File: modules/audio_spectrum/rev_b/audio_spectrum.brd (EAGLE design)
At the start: 68.1 x 66 mm, 86 parts, among them J1 MODULE_GENERIC, J2 AUDIO-JACK-VERTICAL, J7 TC2030-JLINK-L, P1 4k-200k, P2 4k-200k, Q1 NX3008PBK, Q2 NX3008PBK, U1 SAM4LC8AA, U2 MSGEQ7, U3 MSGEQ7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

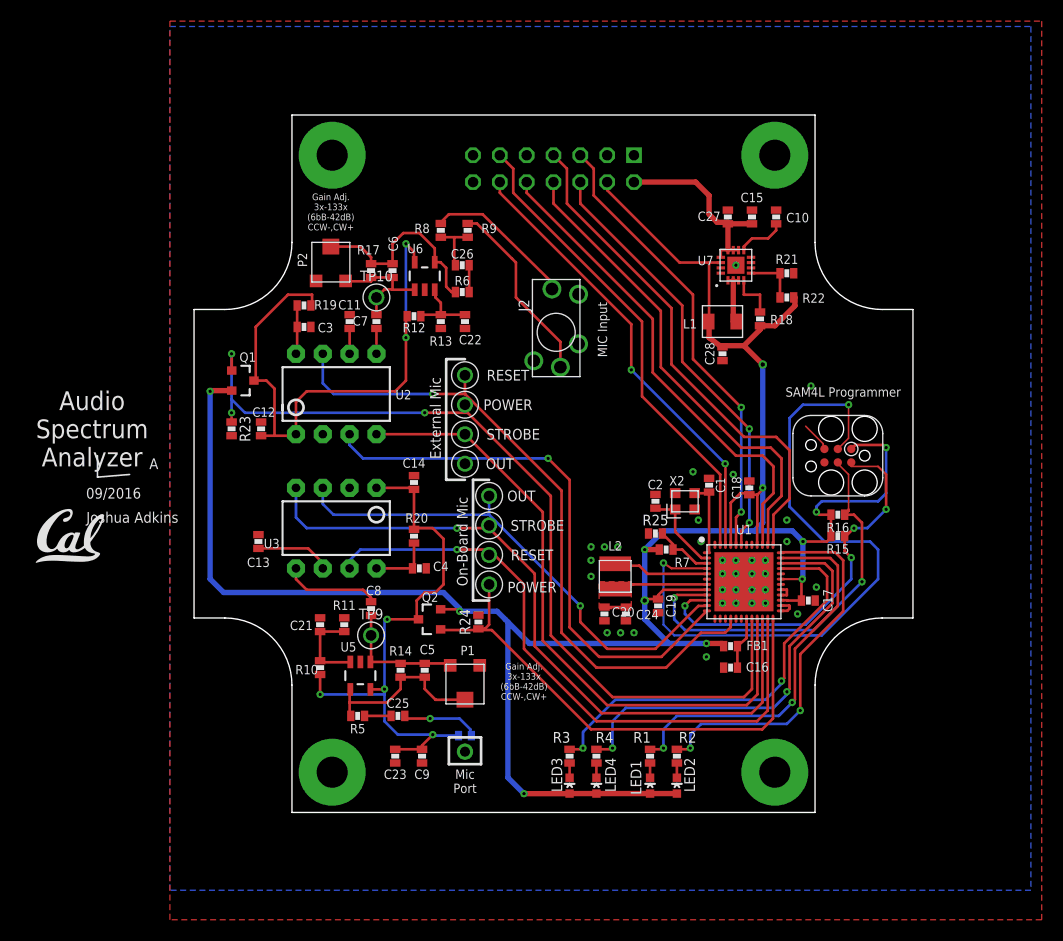
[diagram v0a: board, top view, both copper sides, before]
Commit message: updated audio spectrum board
-fixed the msgeq7 schematic bug
-tried to change layout of the switching stuff
-added some more dnp/populate messages
-added testpoints
-generally rerouted some traces
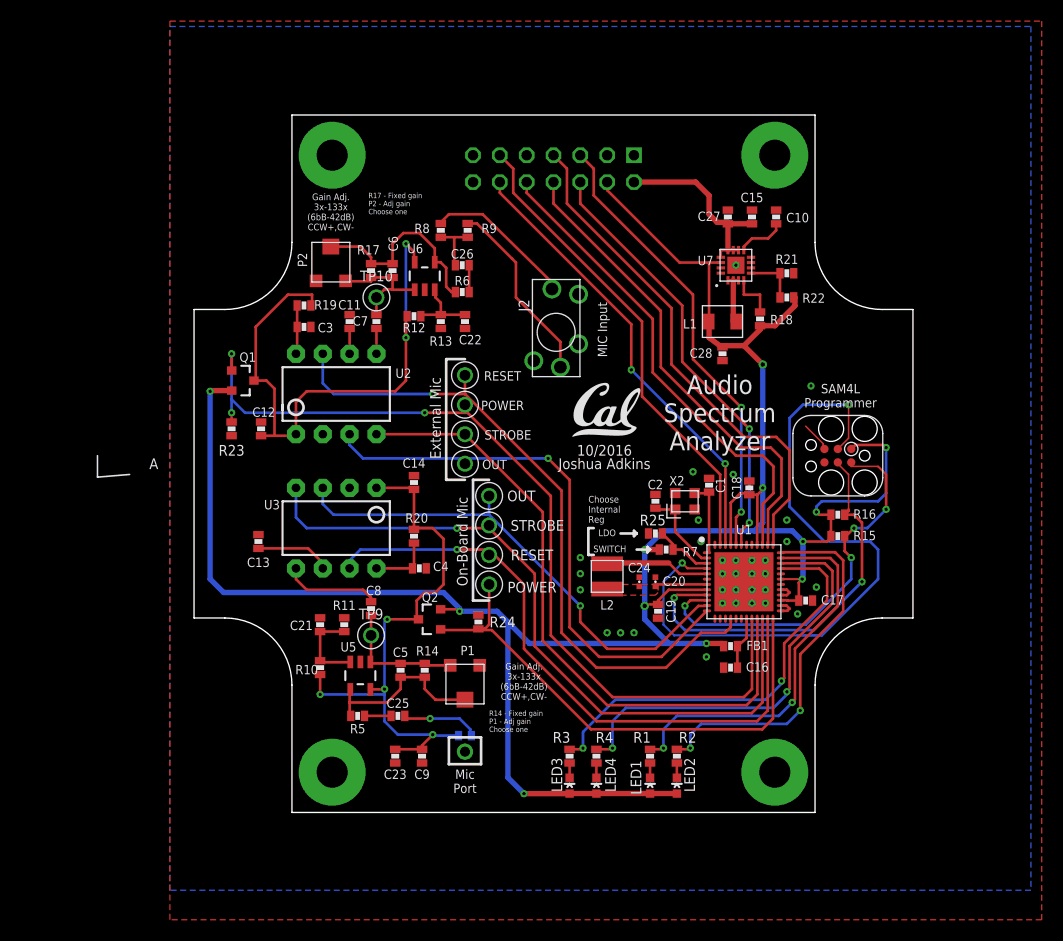
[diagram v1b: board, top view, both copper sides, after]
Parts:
- C20, C24: device passives:0603_CAP -> passives:0402_CAP
- moved U$2 52.2 mm to (38.4, 38.1)
- moved C20 5.71 mm to (46.2, 24.4), turned to 90 degrees
- moved C24 3.30 mm to (44.7, 24.4), turned to 90 degrees
- moved C5 2.29 mm to (22.1, 16.0)
- moved R14 2.29 mm to (24.4, 16.0)
- moved L2 0.76 mm to (41.7, 24.9)
- moved C19 0.51 mm to (46.5, 21.6)
- moved C17 0.25 mm to (60.5, 22.6)
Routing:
- net N$44: track 10.8 -> 4.95 mm
- net !CONTROLLER_RESET: track 65.1 -> 64.1 mm
- net N$52: track 9.09 -> 10.0 mm
- net GND: vias 39 -> 37
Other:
- board text added: "10/2016"
- board text added: "Choose Internal Reg"
- board text added: "Gain Adj. 3x-133x (6bB-42dB) CCW+,CW-"
- board text added: "LDO"
- board text added: "R14 - Fixed gain P1 - Adj gain Choose one"
- board text added: "R17 - Fixed gain P2 - Adj gain Choose one"
- board text added: "SWITCH"
- board text removed: "09/2016"
- board text removed: "Gain Adj. 3x-133x (6bB-42dB) CCW-,CW+"

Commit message: updated audio board layout
-added reset button
-more testpoints
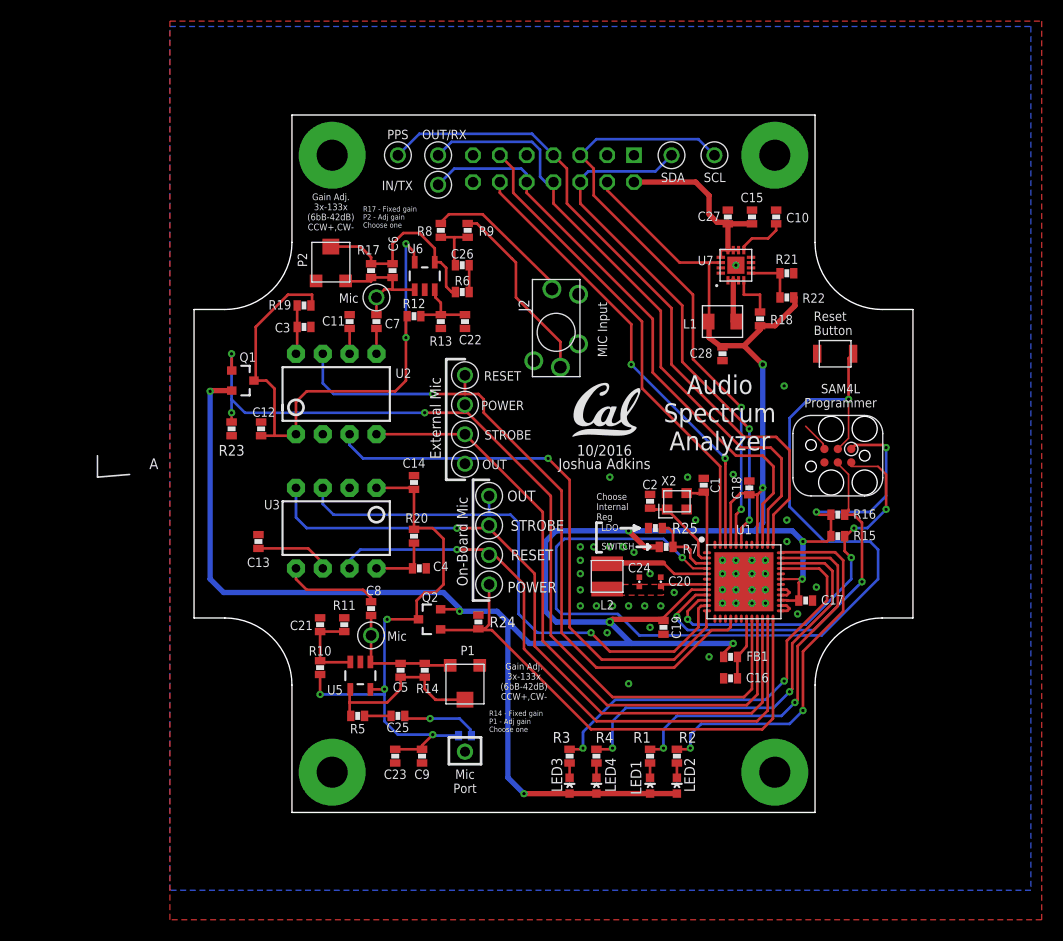
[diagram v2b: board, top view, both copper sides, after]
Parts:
- added S1: B3U-1000P, switches:B3U-1000P
- added TP12, TP13, TP14, TP15, TP16: TEST_POINT_0.040IN, headers:TESTPOINT_0.040IN
- moved C19 1.61 mm to (47.0, 20.1)
- moved FB1 1.02 mm to (53.3, 17.3)
- moved C16 1.02 mm to (53.3, 15.2)
- moved X2 0.76 mm to (48.3, 32.0)
- moved C1 0.51 mm to (50.8, 33.5)
- moved C2 0.51 mm to (45.7, 32.0)
- moved R25 0.51 mm to (46.2, 29.5)
- moved C20 0.51 mm to (46.7, 24.4)
- moved R7 0.25 mm to (47.2, 27.7)
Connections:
- net !CONTROLLER_RESET: now also S1.2
- net GND: now also S1.1
- net MOD_IN: now also TP14.TESTPOINT
- net MOD_OUT: now also TP15.TESTPOINT
- net PPS: now also TP16.TESTPOINT
- net SCL: now also TP12.TESTPOINT
- net SDA: now also TP13.TESTPOINT
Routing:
- net !CONTROLLER_RESET: track 64.1 -> 92.5 mm
- net 3V3: track 235.3 -> 258.9 mm
- net PPS: track 48.6 -> 65.0 mm
- net MOD_OUT: track 45.5 -> 60.0 mm
- net SCL: track 43.4 -> 57.4 mm
- net MOD_IN: track 46.0 -> 55.9 mm
- net SDA: track 41.3 -> 51.1 mm
- net SPEC_OUT: track 48.0 -> 53.4 mm
- net CONTROLLER_SWDCLK: track 38.4 -> 37.0 mm
- net CONTROLLER_BUCK/LDO_N: track 5.70 -> 6.87 mm
- net SPEC2_OUT: track 53.7 -> 54.8 mm
- net N$32: track 5.03 -> 5.97 mm
- net SPEC2_RESET: track 64.6 -> 65.4 mm
- net CONTROLLER_SWDIO: track 37.6 -> 37.1 mm
- net N$44: track 4.95 -> 4.45 mm
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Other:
- board text added: "IN/TX"
- board text added: "Mic"
- board text added: "OUT/RX"
- board text added: "PPS"
- board text added: "Reset Button"
- board text added: "SCL"
- board text added: "SDA"

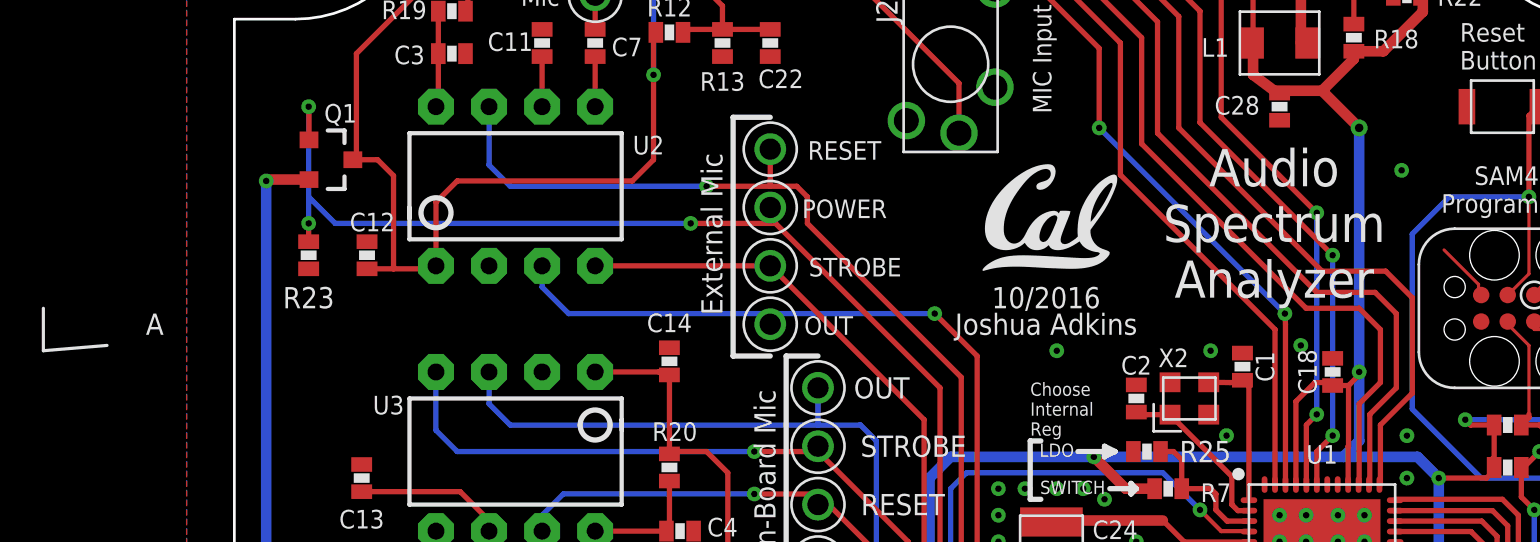
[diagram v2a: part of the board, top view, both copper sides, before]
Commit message: added rev marking
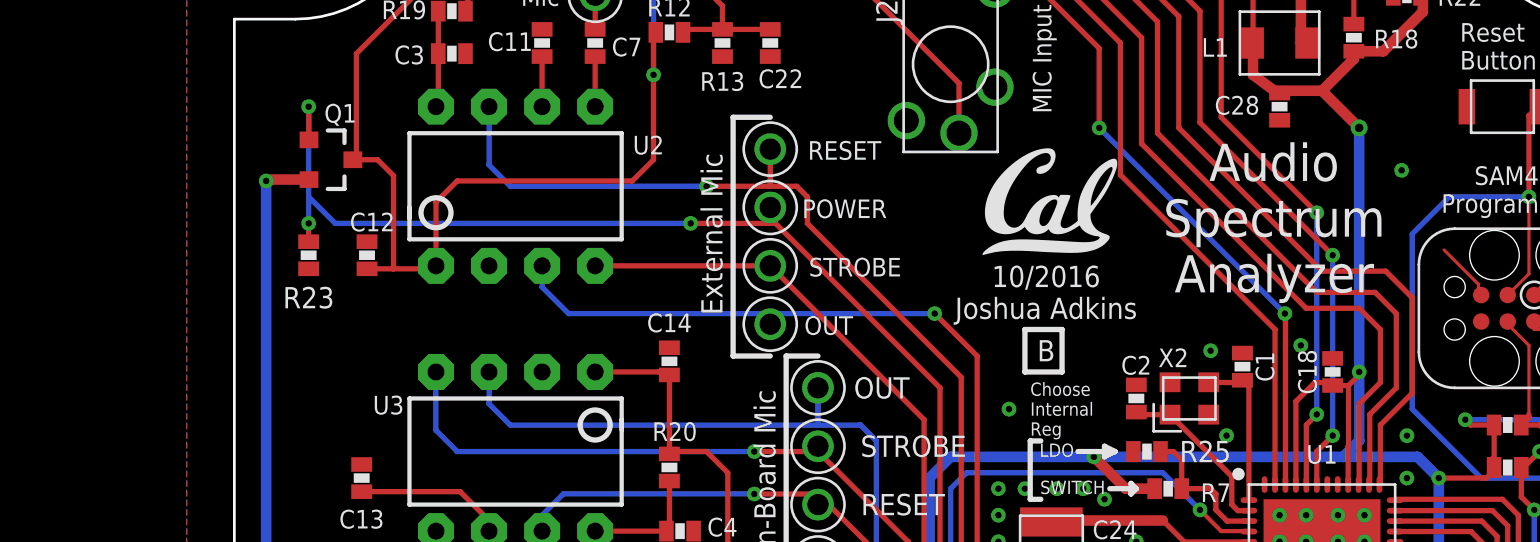
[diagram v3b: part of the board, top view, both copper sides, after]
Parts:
- moved U$2 0.76 mm to (38.4, 38.9)
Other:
- board text added: "B"
- board text removed: "A"
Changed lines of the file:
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@@
 <wire x1="5.461" y1="50.165" x2="11.811" y2="56.515" width="0.127" layer="20" curve="90"/>
 <wire x1="11.811" y1="56.515" x2="11.811" y2="68.58" width="0.127" layer="20"/>
-<text x="52.324" y="36.83" size="1.778" layer="21" font="vector" ratio="12" align="bottom-center">Audio
+<text x="52.324" y="37.084" size="1.778" layer="21" font="vector" ratio="12" align="bottom-center">Audio
 Spectrum
 Analyzer</text>
-<wire x1="-3.556" y1="34.544" x2="-6.604" y2="34.29" width="0.1524" layer="21"/>
-<wire x1="-6.604" y1="34.29" x2="-6.604" y2="36.322" width="0.1524" layer="21"/>
-<text x="-1.27" y="35.052" size="1.016" layer="21" font="vector" ratio="12" align="bottom-center">A</text>
-<text x="41.402" y="35.052" size="1.016" layer="25" font="vector" ratio="12" align="bottom-center">Joshua Adkins</text>
-<text x="41.402" y="36.322" size="1.016" layer="25" font="vector" ratio="12" align="bottom-center">10/2016</text>
+<text x="41.402" y="33.782" size="1.016" layer="21" font="vector" ratio="12" align="bottom-center">B</text>
+<text x="41.402" y="35.814" size="1.016" layer="25" font="vector" ratio="12" align="bottom-center">Joshua Adkins</text>
+<text x="41.402" y="37.338" size="1.016" layer="25" font="vector" ratio="12" align="bottom-center">10/2016</text>
 <text x="31.75" y="43.434" size="0.889" layer="21" font="vector" ratio="12" align="bottom-center">RESET</text>
 <text x="31.75" y="40.64" size="0.889" layer="21" font="vector" ratio="12" align="bottom-center">POWER</text>
@@
 <text x="16.256" y="50.8" size="0.889" layer="21" font="vector" ratio="12">Mic</text>
 <text x="20.828" y="18.796" size="0.889" layer="21" font="vector" ratio="12">Mic</text>
+<wire x1="40.386" y1="35.306" x2="40.386" y2="33.274" width="0.254" layer="21"/>
+<wire x1="40.386" y1="33.274" x2="42.164" y2="33.274" width="0.254" layer="21"/>
+<wire x1="42.164" y1="33.274" x2="42.164" y2="35.306" width="0.254" layer="21"/>
+<wire x1="42.164" y1="35.306" x2="40.386" y2="35.306" width="0.254" layer="21"/>
 </plain>
 <attributes>
@@
 <attribute name="NAME" x="50.152" y="49.254" size="0.889" layer="25" rot="R180"/>
 </element>
-<element name="U$2" library="logos" package="UCB_CAL_200MIL" value="" x="38.354" y="38.1"/>
+<element name="U$2" library="logos" package="UCB_CAL_200MIL" value="" x="38.354" y="38.862"/>
 <element name="J2" library="connector" package="AUDIO-JACK-VERTICAL" value="AUDIO-JACK-VERTICAL" x="36.83" y="48.006" smashed="yes" rot="R90">
 <attribute name="MOUSER" value="806-STX-3790-5N" x="36.83" y="48.006" size="1.778" layer="27" font="vector" ratio="12" rot="R90" display="off"/>
@@
 <via x="45.72" y="25.146" extent="1-16" drill="0.3048"/>
 <contactref element="S1" pad="1"/>
-<via x="41.91" y="34.29" extent="1-16" drill="0.3048"/>
+<via x="39.624" y="31.496" extent="1-16" drill="0.3048"/>
 <via x="43.688" y="14.732" extent="1-16" drill="0.3048"/>
 </signal>

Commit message: moved the inductor a bit closer
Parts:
- moved C20 1.02 mm to (47.8, 24.4)
- moved C24 0.76 mm to (45.5, 24.4)
- moved L2 0.76 mm to (42.4, 24.9)
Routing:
- net N$44: track 4.45 -> 3.63 mm
- net N$52: track 10.0 -> 9.30 mm
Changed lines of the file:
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@@
 <attribute name="NAME" x="55.88" y="17.78" size="0.889" layer="25" font="vector" ratio="12" rot="R180" align="bottom-center"/>
 </element>
-<element name="L2" library="signpost" package="1212" value="22uH" x="41.656" y="24.892" smashed="yes" rot="R90">
-<attribute name="DIGIKEY" value="490-5350-1-ND" x="77.216" y="-10.668" size="1.778" layer="27" font="vector" ratio="12" rot="R90" display="off"/>
-<attribute name="NAME" x="41.656" y="22.638" size="0.889" layer="25" font="vector" ratio="12" rot="R180" align="bottom-center"/>
-</element>
-<element name="C20" library="passives" package="0402_CAP" value="100nF" x="46.736" y="24.384" smashed="yes" rot="R90">
-<attribute name="DIGIKEY" value="490-10777-1-ND" x="74.676" y="-13.716" size="1.778" layer="27" font="vector" ratio="12" rot="R90" display="off"/>
-<attribute name="NAME" x="48.514" y="24.892" size="0.889" layer="25" font="vector" ratio="12" rot="R180" align="bottom-center"/>
-</element>
-<element name="C24" library="passives" package="0402_CAP" value="4.7uF" x="44.704" y="24.384" smashed="yes" rot="R90">
-<attribute name="DIGIKEY" value="490-13252-1-ND" x="77.724" y="-18.796" size="1.778" layer="27" font="vector" ratio="12" rot="R90" display="off"/>
-<attribute name="NAME" x="44.704" y="26.162" size="0.889" layer="25" font="vector" ratio="12" rot="R180" align="bottom-center"/>
+<element name="L2" library="signpost" package="1212" value="22uH" x="42.418" y="24.892" smashed="yes" rot="R90">
+<attribute name="DIGIKEY" value="490-5350-1-ND" x="77.978" y="-10.668" size="1.778" layer="27" font="vector" ratio="12" rot="R90" display="off"/>
+<attribute name="NAME" x="42.418" y="22.638" size="0.889" layer="25" font="vector" ratio="12" rot="R180" align="bottom-center"/>
+</element>
+<element name="C20" library="passives" package="0402_CAP" value="100nF" x="47.752" y="24.384" smashed="yes" rot="R90">
+<attribute name="DIGIKEY" value="490-10777-1-ND" x="75.692" y="-13.716" size="1.778" layer="27" font="vector" ratio="12" rot="R90" display="off"/>
+<attribute name="NAME" x="47.752" y="23.368" size="0.889" layer="25" font="vector" ratio="12" rot="R180" align="bottom-center"/>
+</element>
+<element name="C24" library="passives" package="0402_CAP" value="4.7uF" x="45.466" y="24.384" smashed="yes" rot="R90">
+<attribute name="DIGIKEY" value="490-13252-1-ND" x="78.486" y="-18.796" size="1.778" layer="27" font="vector" ratio="12" rot="R90" display="off"/>
+<attribute name="NAME" x="45.72" y="26.162" size="0.889" layer="25" font="vector" ratio="12" rot="R180" align="bottom-center"/>
 </element>
 <element name="J1" library="signpost" package="MODULE_GENERIC" value="MODULE_GENERIC" x="36.576" y="35.56" smashed="yes">
@@
 <via x="43.18" y="27.686" extent="1-16" drill="0.3048"/>
 <via x="45.72" y="20.066" extent="1-16" drill="0.3048"/>
-<via x="48.006" y="23.368" extent="1-16" drill="0.3048"/>
+<via x="47.752" y="22.86" extent="1-16" drill="0.3048"/>
 <via x="42.164" y="22.098" extent="1-16" drill="0.3048"/>
 <via x="40.64" y="22.098" extent="1-16" drill="0.3048"/>
-<via x="44.196" y="27.178" extent="1-16" drill="0.3048"/>
-<via x="45.72" y="25.146" extent="1-16" drill="0.3048"/>
+<via x="44.45" y="27.178" extent="1-16" drill="0.3048"/>
+<via x="46.482" y="25.146" extent="1-16" drill="0.3048"/>
 <contactref element="S1" pad="1"/>
 <via x="39.624" y="31.496" extent="1-16" drill="0.3048"/>
@@
 <contactref element="C20" pad="1"/>
 <contactref element="U1" pad="7"/>
-<wire x1="51.11" y1="24.134" x2="46.91906875" y2="24.134" width="0.254" layer="1"/>
+<wire x1="51.11" y1="24.134" x2="47.68106875" y2="24.134" width="0.254" layer="1"/>
 <polygon width="0.254" layer="1" isolate="0.3048" thermals="no">
-<vertex x="40.386" y="23.114"/>
-<vertex x="40.386" y="24.13"/>
-<vertex x="46.99" y="24.13"/>
+<vertex x="41.148" y="23.114"/>
+<vertex x="41.148" y="24.13"/>
+<vertex x="48.006" y="24.13"/>
+<vertex x="48.006" y="23.622"/>
+<vertex x="46.99" y="23.622"/>
 <vertex x="46.99" y="23.114"/>
 </polygon>
-<wire x1="46.91906875" y1="24.134" x2="46.736" y2="23.95093125" width="0.254" layer="1"/>
+<wire x1="47.68106875" y1="24.134" x2="47.752" y2="23.95093125" width="0.254" layer="1"/>
 </signal>
 <signal name="N$52">
 <contactref element="L2" pad="P$2"/>
 <contactref element="U1" pad="5"/>
-<wire x1="41.656" y1="26.092" x2="42.602" y2="25.908" width="0.254" layer="1"/>
-<wire x1="51.11" y1="25.134" x2="48.018" y2="25.134" width="0.254" layer="1"/>
-<wire x1="48.018" y1="25.134" x2="46.99" y2="26.162" width="0.254" layer="1"/>
-<wire x1="46.99" y1="26.162" x2="42.856" y2="26.162" width="0.508" layer="1"/>
+<wire x1="42.418" y1="26.092" x2="42.602" y2="25.908" width="0.254" layer="1"/>
+<wire x1="51.11" y1="25.134" x2="49.034" y2="25.134" width="0.254" layer="1"/>
+<wire x1="49.034" y1="25.134" x2="48.006" y2="26.162" width="0.254" layer="1"/>
+<wire x1="48.006" y1="26.162" x2="42.856" y2="26.162" width="0.508" layer="1"/>
 <wire x1="42.856" y1="26.162" x2="42.602" y2="25.908" width="0.254" layer="1"/>
 </signal>
